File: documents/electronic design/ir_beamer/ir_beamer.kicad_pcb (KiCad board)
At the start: 2 copper layers, 40 parts, among them P1 CONN_01X01, P10 CONN_01X01, P11 CONN_01X01, P2 CONN_01X01, P3 CONN_01X01, P4 CONN_01X01, P5 CONN_01X01, P6 CONN_01X01, P7 CONN_01X01, P8 CONN_01X01, P9 CONN_01X01, T1 2N7002K, T10 2N7002K, T11 2N7002K, T2 2N7002K, T3 2N7002K, T4 2N7002K, T5 2N7002K, T6 2N7002K, T7 2N7002K, T8 2N7002K, T9 2N7002K, U1 74HC595D, U2 STM32F103HEADER, U3 74HC595D

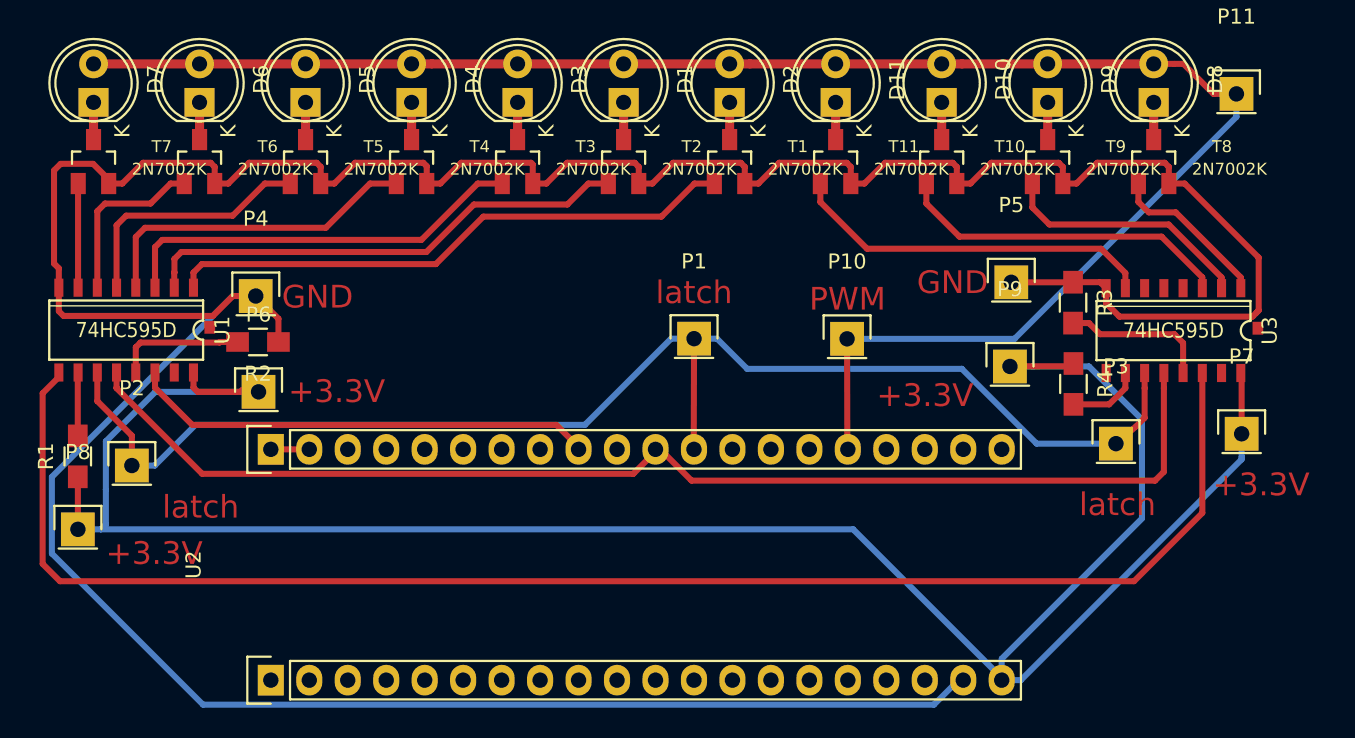
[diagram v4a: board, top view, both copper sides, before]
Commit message: create new pcb project for ir receiver
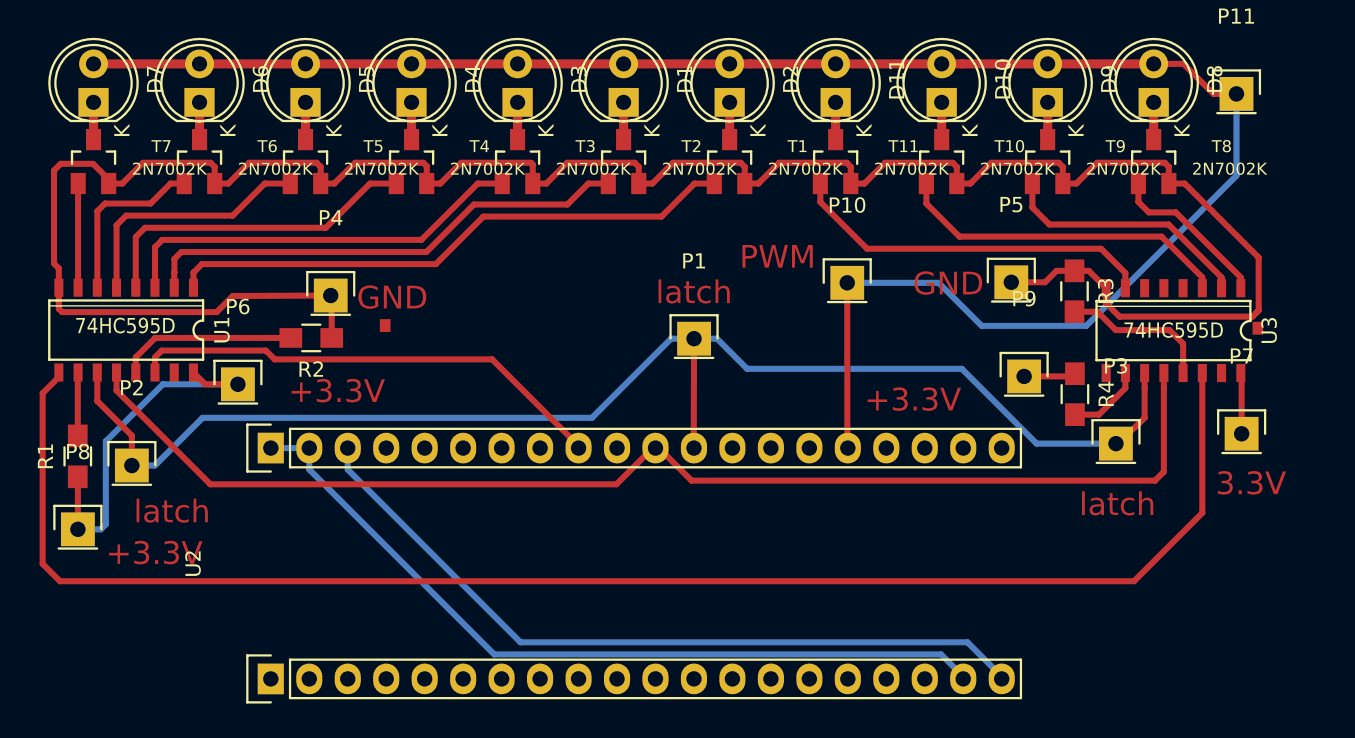
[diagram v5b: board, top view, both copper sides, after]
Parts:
- moved P4 4.95 mm to (35.0, 31.9)
- moved P10 3.70 mm to (69.1, 31.1)
- moved R2 3.53 mm to (33.8, 34.7)
- moved P6 1.45 mm to (28.9, 37.8)
- moved P9 1.15 mm to (80.8, 37.2)
- moved R3 0.76 mm to (84.2, 31.6)
- moved R4 0.68 mm to (84.2, 38.4)
- moved U2 0.08 mm to (31.1, 57.2)
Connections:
- U2 pad 19: GND -> Net-(U2-Pad19)
- U2 pad 20: +3V3 -> Net-(U2-Pad20)
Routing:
- net +3V3: track 154.8 -> 32.2 mm
- net GND: track 239.8 -> 153.1 mm
- net Net-(U2-Pad19): track 0.00 -> 53.4 mm
- net Net-(U2-Pad20): track 0.00 -> 50.7 mm
- net IR_PWM: track 116.9 -> 123.7 mm
- net Net-(R2-Pad2): track 8.53 -> 11.8 mm
- net SPI_MOSI: track 30.7 -> 32.2 mm
- net SPI_SCK: track 81.1 -> 81.9 mm
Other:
- board text added: "3.3V"

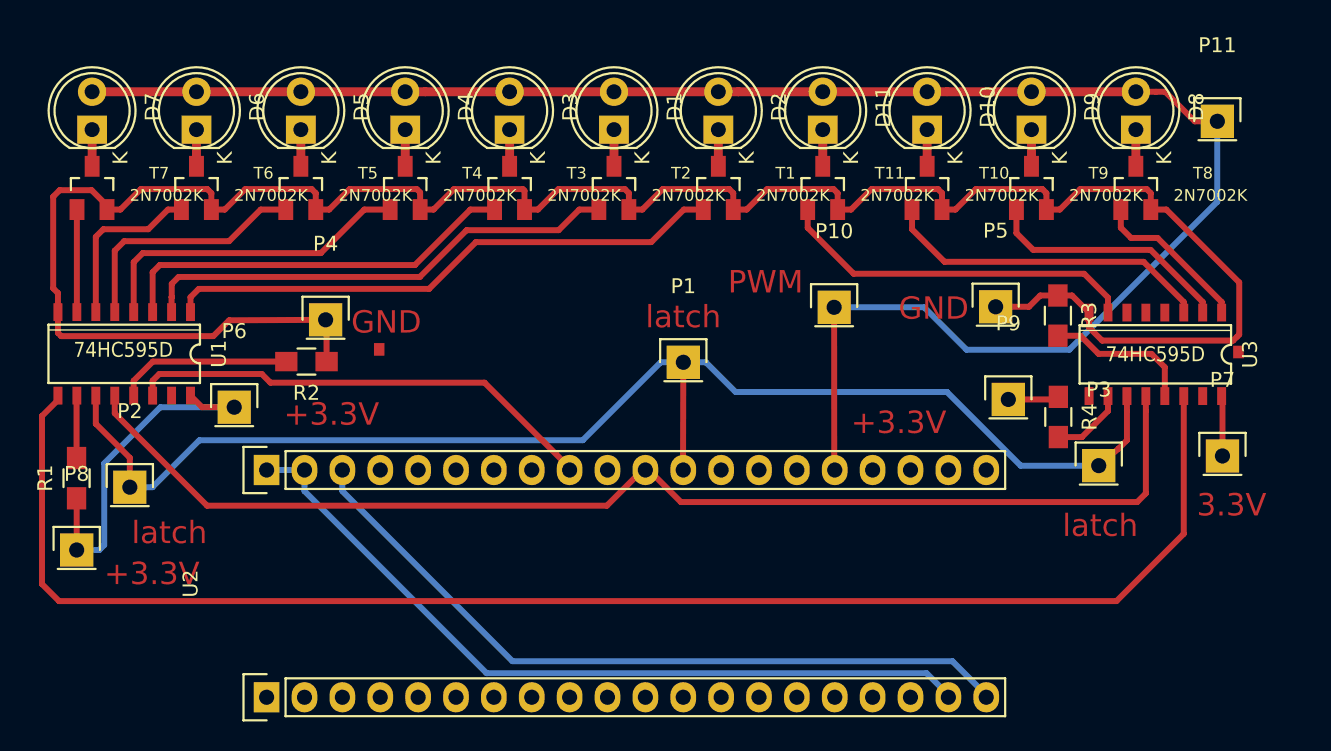
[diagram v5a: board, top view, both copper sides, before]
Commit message: make double sided pcb for beamer
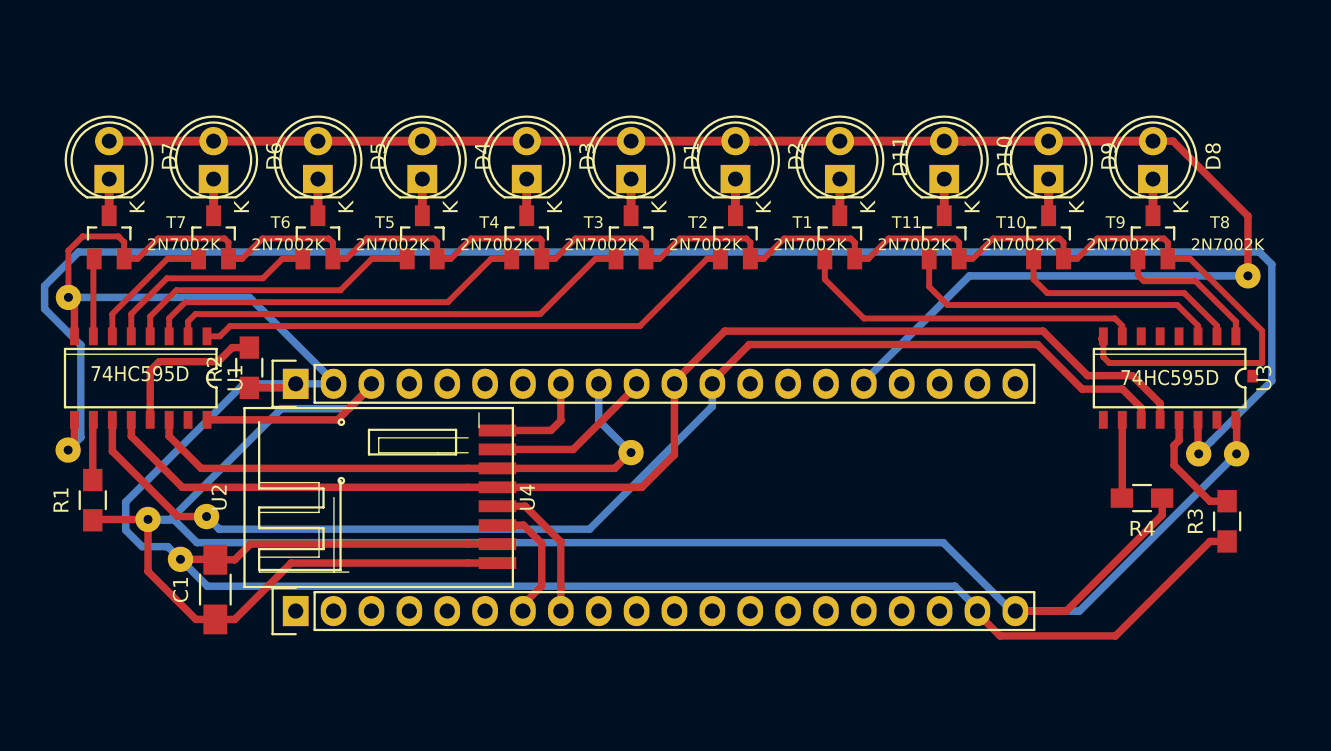
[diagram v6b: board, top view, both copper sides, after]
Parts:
- removed P11, P6: CONN_01X01, Pin_Headers:Pin_Header_Straight_1x01
- added C1: 100uf, Capacitors_SMD:C_1206_HandSoldering, F.Cu at (27.7, 50.0)
- added U4: SE8R01_module, footprints:SE8R01_SMD, F.Cu at (47.6, 49.8)
- P1, P10, P2, P3, P4, P5, P7, P8, P9: value CONN_01X01 -> Via; footprint Pin_Headers:Pin_Header_Straight_1x01 -> footprints:Via
- R1, R2, R3, R4: value R -> 4.7k
- moved P5 58.6 mm to (23.1, 45.3)
- moved P10 51.4 mm to (17.8, 30.4)
- moved P4 18.8 mm to (25.3, 48.0)
- moved R3 17.9 mm to (95.5, 45.4), turned to 90 degrees
- moved P3 16.2 mm to (96.9, 29.0)
- moved P9 15.7 mm to (96.1, 40.9)
- moved R4 7.82 mm to (89.8, 43.9), turned to 180 degrees
- moved P1 7.00 mm to (55.5, 40.8)
- moved P8 6.72 mm to (17.8, 40.6)
- moved U2 6.10 mm to (33.0, 51.4)
- moved P2 5.51 mm to (27.1, 45.1)
- moved R2 3.86 mm to (29.9, 35.1), turned to 90 degrees
- moved D10 3.51 mm to (76.5, 22.5)
- moved D11 3.51 mm to (69.5, 22.5)
- moved D8 3.51 mm to (90.5, 22.5)
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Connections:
- P1 pad 1: Latch -> SPI_MOSI
- P10 pad 1: IR_PWM -> GND
- P3 pad 1: Latch -> IR_PWM
- P5 pad 1: GND -> +3V3
- P7 pad 1: +3V3 -> Net-(P7-Pad1)
- P8 pad 1: +3V3 -> Net-(P7-Pad1)
- U1 pad 9: Net-(U1-Pad9) -> Net-(P7-Pad1)
- U2 pad 19: Net-(U2-Pad19) -> GND
- U2 pad 20: Net-(U2-Pad20) -> +3V3
- U2 pad 28: Net-(U2-Pad28) -> SE8R01_IRQ
- U2 pad 30: Net-(U2-Pad30) -> SPI_MISO
- U2 pad 7: Net-(U2-Pad7) -> SE8R01_CE
- U2 pad 8: Net-(U2-Pad8) -> SE8R01_CSN
- U3 pad 14: Net-(U1-Pad9) -> Net-(P7-Pad1)
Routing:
- net +3V3: track 32.2 -> 161.6 mm
- net Net-(P7-Pad1): track 0.00 -> 115.6 mm
- net GND: track 153.1 -> 266.7 mm
- net Net-(U1-Pad9): track 101.2 -> 0.00 mm
- net Net-(U2-Pad19): track 53.4 -> 0.00 mm
- net Net-(U2-Pad20): track 50.7 -> 0.00 mm
- net IR_PWM: track 123.7 -> 111.3 mm
- net SPI_MISO: track 0.00 -> 11.2 mm
- net SE8R01_CSN: track 0.00 -> 9.87 mm
- net Latch: track 91.2 -> 82.1 mm
- net SE8R01_CE: track 0.00 -> 8.53 mm
- net SE8R01_IRQ: track 0.00 -> 6.98 mm
- net SPI_MOSI: track 32.2 -> 38.9 mm
- net IR_LED_6: track 11.5 -> 8.81 mm
- net Net-(R3-Pad2): track 9.98 -> 7.74 mm
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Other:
- net class Default: trace_width 0.4 -> 0.5
- board text removed: "+3.3V"
- board text removed: "3.3V"
- board text removed: "GND"
- board text removed: "PWM"
- board text removed: "latch"

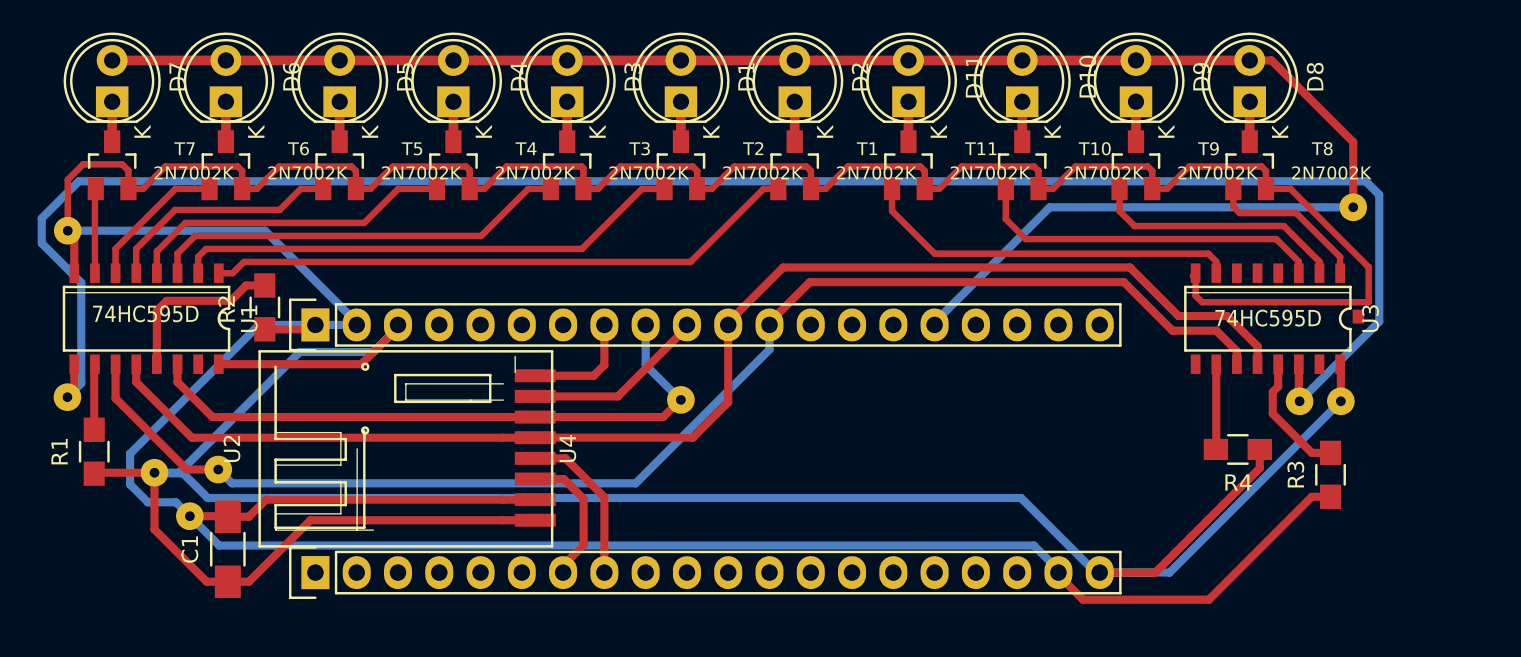
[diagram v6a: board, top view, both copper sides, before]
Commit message: update pcb for beamer (use 5V to drive LED)
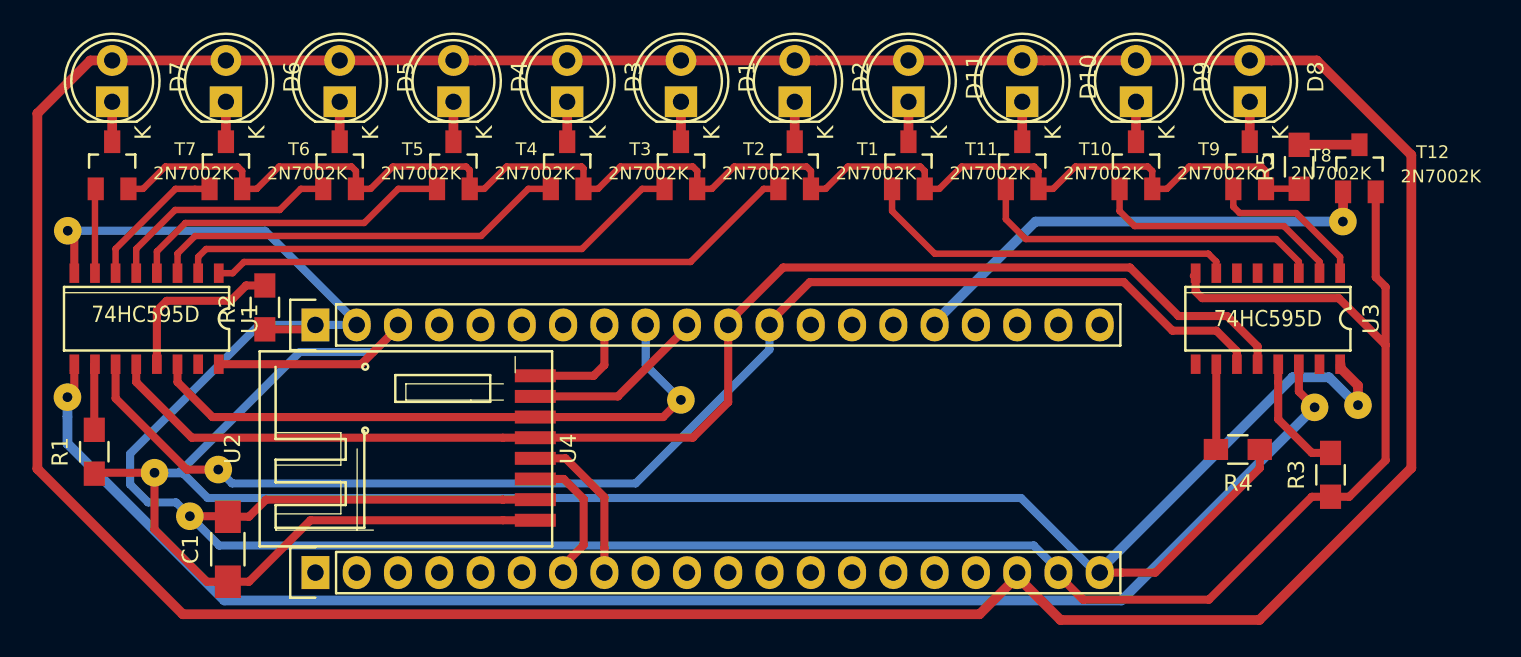
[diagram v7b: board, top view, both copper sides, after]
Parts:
- added R5: 100, Resistors_SMD:R_0805_HandSoldering, F.Cu at (93.6, 26.5)
- added T12: 2N7002K, footprints:SOT23, F.Cu at (97.3, 26.6)
- moved P3 1.09 mm to (96.3, 29.8)
- moved P9 1.08 mm to (97.2, 41.1)
- moved P7 1.00 mm to (94.5, 41.3)
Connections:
- D1 pad 2: IR_PWM -> +5V
- D10 pad 2: IR_PWM -> +5V
- D11 pad 2: IR_PWM -> +5V
- D2 pad 2: IR_PWM -> +5V
- D3 pad 2: IR_PWM -> +5V
- D4 pad 2: IR_PWM -> +5V
- D5 pad 2: IR_PWM -> +5V
- D6 pad 2: IR_PWM -> +5V
- D7 pad 2: IR_PWM -> +5V
- D8 pad 2: IR_PWM -> +5V
- D9 pad 2: IR_PWM -> +5V
- T1 pad 2: GND -> PWM_GND
- T10 pad 2: GND -> PWM_GND
- T11 pad 2: GND -> PWM_GND
- T2 pad 2: GND -> PWM_GND
- T3 pad 2: GND -> PWM_GND
- T4 pad 2: GND -> PWM_GND
- T5 pad 2: GND -> PWM_GND
- T6 pad 2: GND -> PWM_GND
- T7 pad 2: GND -> PWM_GND
- T8 pad 2: GND -> PWM_GND
- T9 pad 2: GND -> PWM_GND
- U1 pad 15: Net-(U1-Pad15) -> (no net)
- U2 pad 1: Net-(U2-Pad1) -> (no net)
- U2 pad 10: Net-(U2-Pad10) -> (no net)
- U2 pad 11: Net-(U2-Pad11) -> (no net)
- U2 pad 12: Net-(U2-Pad12) -> (no net)
- U2 pad 13: Net-(U2-Pad13) -> (no net)
- U2 pad 14: Net-(U2-Pad14) -> (no net)
- U2 pad 15: Net-(U2-Pad15) -> (no net)
- U2 pad 16: Net-(U2-Pad16) -> (no net)
- U2 pad 17: Net-(U2-Pad17) -> (no net)
- U2 pad 18: Net-(U2-Pad18) -> +5V
- U2 pad 2: Net-(U2-Pad2) -> (no net)
- U2 pad 24: Net-(U2-Pad24) -> (no net)
- U2 pad 25: Net-(U2-Pad25) -> (no net)
- U2 pad 26: Net-(U2-Pad26) -> (no net)
- U2 pad 27: Net-(U2-Pad27) -> (no net)
- U2 pad 3: Net-(U2-Pad3) -> (no net)
- U2 pad 33: Net-(U2-Pad33) -> (no net)
- U2 pad 34: Net-(U2-Pad34) -> (no net)
- U2 pad 35: Net-(U2-Pad35) -> (no net)
- U2 pad 37: Net-(U2-Pad37) -> (no net)
- U2 pad 38: Net-(U2-Pad38) -> (no net)
- U2 pad 39: Net-(U2-Pad39) -> (no net)
- U2 pad 4: Net-(U2-Pad4) -> (no net)
- U2 pad 40: Net-(U2-Pad40) -> (no net)
- U2 pad 5: Net-(U2-Pad5) -> (no net)
- U2 pad 6: Net-(U2-Pad6) -> (no net)
- U2 pad 9: Net-(U2-Pad9) -> (no net)
- U3 pad 15: Net-(U3-Pad15) -> (no net)
- U3 pad 4: Net-(U3-Pad4) -> (no net)
- U3 pad 5: Net-(U3-Pad5) -> (no net)
- U3 pad 6: Net-(U3-Pad6) -> (no net)
- U3 pad 9: Net-(U3-Pad9) -> (no net)
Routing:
- net +5V: track 0.00 -> 223.9 mm
- net PWM_GND: track 0.00 -> 90.2 mm
- net GND: track 266.7 -> 182.6 mm
- net IR_PWM: track 111.3 -> 29.7 mm
- net Net-(P7-Pad1): track 115.6 -> 94.2 mm
- net Net-(R5-Pad2): track 0.00 -> 3.72 mm
- net +3V3: track 161.6 -> 164.8 mm
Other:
- net class Default: trace_width 0.5 -> 0.4
- board text removed: "."
